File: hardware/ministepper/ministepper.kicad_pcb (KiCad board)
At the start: 4 copper layers, 0 parts

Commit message: hardware: scaffold ministepper (TMC2130 dual stepper driver) project
Third PCB in the family, matching firmware/tsumikoro-ministepper's
STM32G071G8U6 target. 4-layer, same JLC04161H stackup and design rules
as servo + bridge.

Placed (not wired):
- U1 STM32G071G8U6 UFQFPN-28 (core MCU)
- U2, U3 TMC2130-LA-T (shared SPI bus, per-driver CS/STEP/DIR/EN/DIAG)
- U4 SIT3088EEUA (RS-485, USART2 on PA2/PA3 — no SYSCFG remap needed on
  G071 unlike G030)
- JBUS1, JBUS2 (JST-XH 4-pin daisy-chain, V+/B/A/GND)
- JMOT1, JMOT2 (JST-XH 4-pin stepper outputs)
- JPWR (JST-XH 2-pin optional external motor supply)
- D1, D2 (SS34 Schottky diode-OR for bus V+ vs external)

PSU sub-sheet forked from servo's psu.kicad_sch — TPS54061 @ 3.3V,
sized for ~150 mA (MCU + 2x TMC VCC_IO + RS-485). UUIDs retargeted for
the ministepper project.

Docs README covers the full pin map, TMC2130 strapping checklist
(sense resistors, charge pump cap, VCP/5VOUT/VCC caps, DIAG pull-ups),
connectors, and regeneration commands.

Added hardware/TODO.md tracking servo/bridge/ministepper/light-sensor
projects with outstanding work per board.

Makefile PROJECTS list extended to servo bridge ministepper.
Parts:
- added C1: 2.2uF, Capacitor_SMD:C_1206_3216Metric, F.Cu at (170.7, 75.6)
- added C2: 100nF, Capacitor_SMD:C_0603_1608Metric, F.Cu at (169.9, 78.5)
- added C3: 100nF, Capacitor_SMD:C_0402_1005Metric, F.Cu at (160.9, 87.0)
- added C4: 10uF, Capacitor_SMD:C_0805_2012Metric, F.Cu at (167.3, 82.0)
- added C5: 10uF, Capacitor_SMD:C_0805_2012Metric, F.Cu at (167.3, 85.0)
- added D1: MBRD10200, Package_TO_SOT_SMD:TO-252-2, F.Cu at (152.2, 94.8)
- added D2: MBRD10200, Package_TO_SOT_SMD:TO-252-2, F.Cu at (152.2, 103.0)
- added JBUS1: Conn_01x04_XH, Connector_JST:JST_XH_S4B-XH-A_1x04_P2.50mm_Horizontal, F.Cu at (134.3, 94.0)
- added JBUS2: Conn_01x04_XH, Connector_JST:JST_XH_S4B-XH-A_1x04_P2.50mm_Horizontal, F.Cu at (134.3, 107.5)
- added JDC1: DC-005 2.0mm, Connector_BarrelJack:BarrelJack_GCT_DCJ200-10-A_Horizontal, F.Cu at (119.2, 75.9)
- added JDC2: DC-005 2.0mm, Connector_BarrelJack:BarrelJack_GCT_DCJ200-10-A_Horizontal, F.Cu at (131.6, 75.9)
- added JPTERM1: TERM1, Jumper:SolderJumper-2_P1.3mm_Open_Pad1.0x1.5mm, F.Cu at (154.7, 84.9)
- added JPTERM2: TERM2, Jumper:SolderJumper-2_P1.3mm_Open_Pad1.0x1.5mm, F.Cu at (154.7, 88.4)
- added J_USB2: USB-TYPE-C-019, Connector_USB:USB_C_Receptacle_GCT_USB4105-xx-A_16P_TopMnt_Horizontal, F.Cu at (151.1, 112.3)
- added L1: 10uH, Inductor_SMD:L_Changjiang_FNR4030S, F.Cu at (162.2, 83.3)
- added R1: 100k, Resistor_SMD:R_0402_1005Metric, F.Cu at (171.0, 81.5)
- added R2: 22k, Resistor_SMD:R_0402_1005Metric, F.Cu at (171.0, 83.5)
- added R3: 10k, Resistor_SMD:R_0402_1005Metric, F.Cu at (171.0, 85.5)
- added R4: 120R, Resistor_SMD:R_1206_3216Metric, F.Cu at (149.8, 84.8)
- added R5: 120R, Resistor_SMD:R_1206_3216Metric, F.Cu at (149.8, 88.1)
- added R_BOOT2: 10k, Resistor_SMD:R_0402_1005Metric, F.Cu at (155.8, 74.9)
- added R_CC1: 5.1k, Resistor_SMD:R_0402_1005Metric, F.Cu at (155.8, 76.9)
- added R_CC2: 5.1k, Resistor_SMD:R_0402_1005Metric, F.Cu at (155.8, 78.9)
- added R_EN2: 10k, Resistor_SMD:R_0402_1005Metric, F.Cu at (155.8, 80.9)
- added SW_BOOT2: BOOT, tsumikoro:SW_Push_1P1T_XKB_TS-1187A, F.Cu at (142.7, 77.2)
- added SW_RESET2: RESET, tsumikoro:SW_Push_1P1T_XKB_TS-1187A, F.Cu at (142.7, 83.9)
- added U1: SIT3088EEUA, Package_SO:MSOP-8_3x3mm_P0.65mm, F.Cu at (150.7, 76.2)
- added U2: LMR38020SDDAR, Package_SO:SOIC-8-1EP_3.9x4.9mm_P1.27mm_EP2.29x3mm, F.Cu at (163.6, 77.3)
- added U3: SIT3088EEUA, Package_SO:MSOP-8_3x3mm_P0.65mm, F.Cu at (150.7, 80.8)
- added U4: ESP32-S3-MINI-1-N8, tsumikoro:ESP32-S3-MINI-1, F.Cu at (186.6, 117.8)

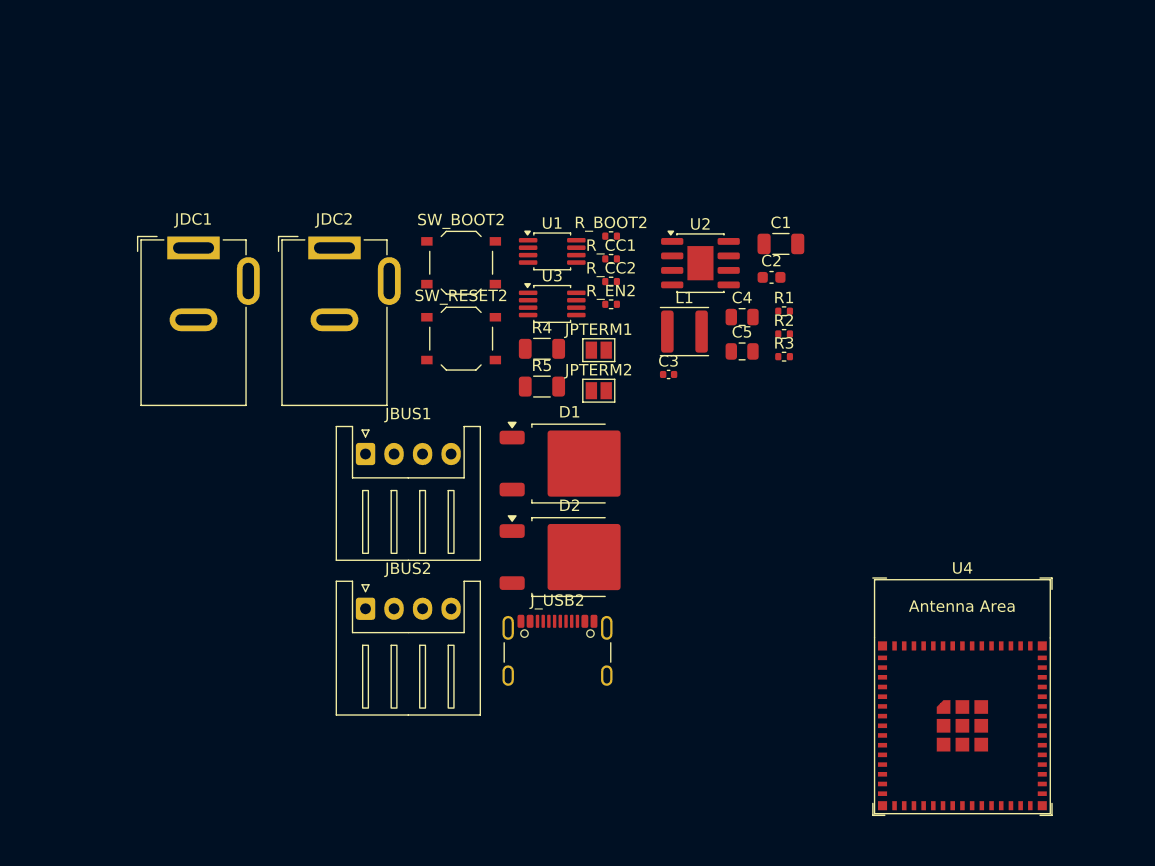
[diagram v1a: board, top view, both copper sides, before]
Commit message: ministepper: motor connectors (JMOT1, JMOT2) switch to vertical JST-XH
Was S4B-XH-A horizontal (right-angle, LCSC C157925) — now B4B-XH-A
vertical (top-mount, LCSC C595709, B4B-XH-A-R(LF)(SN), red housing
version, ~$0.08). The vertical variant keeps the motor cables exiting
straight up, which is usually more natural for stepper wiring vs the
board-edge horizontal style.

Bus connectors (JBUS1, JBUS2) and the optional external-power input
(JPWR) remain horizontal S*B-XH-A for board-edge cable exit.

Also regenerates docs + JLCPCB package.
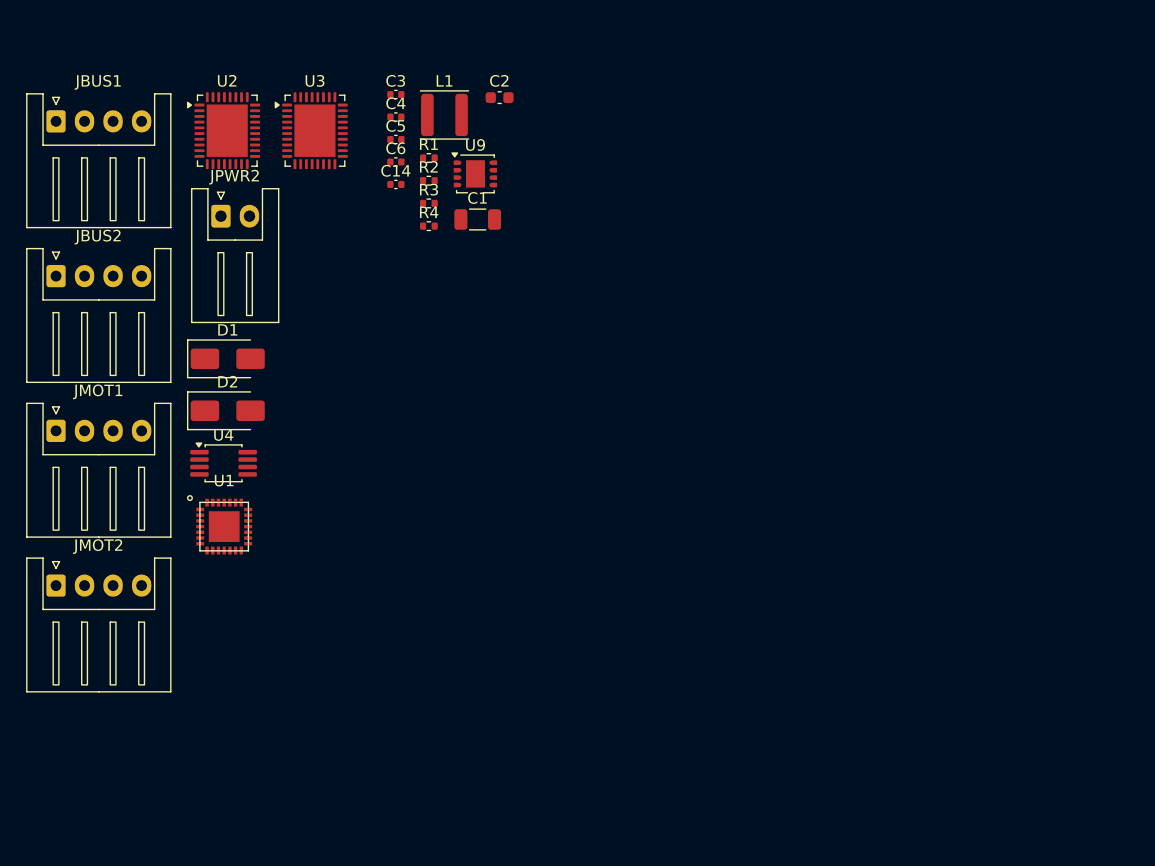
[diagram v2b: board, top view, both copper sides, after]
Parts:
- removed JDC1, JDC2: DC-005 2.0mm, Connector_BarrelJack:BarrelJack_GCT_DCJ200-10-A_Horizontal
- removed JPTERM1: TERM1, Jumper:SolderJumper-2_P1.3mm_Open_Pad1.0x1.5mm
- removed JPTERM2: TERM2, Jumper:SolderJumper-2_P1.3mm_Open_Pad1.0x1.5mm
- removed J_USB2: USB-TYPE-C-019, Connector_USB:USB_C_Receptacle_GCT_USB4105-xx-A_16P_TopMnt_Horizontal
- removed R5: 120R, Resistor_SMD:R_1206_3216Metric
- removed R_BOOT2, R_EN2: 10k, Resistor_SMD:R_0402_1005Metric
- removed R_CC1, R_CC2: 5.1k, Resistor_SMD:R_0402_1005Metric
- removed SW_BOOT2: BOOT, tsumikoro:SW_Push_1P1T_XKB_TS-1187A
- removed SW_RESET2: RESET, tsumikoro:SW_Push_1P1T_XKB_TS-1187A
- added C14: 10uF, Capacitor_SMD:C_0402_1005Metric, F.Cu at (137.0, 70.4)
- added C6: 33pF, Capacitor_SMD:C_0402_1005Metric, F.Cu at (137.0, 68.4)
- added JMOT1: Stepper 1, Connector_JST:JST_XH_S4B-XH-A_1x04_P2.50mm_Horizontal, F.Cu at (107.2, 92.0)
- added JMOT2: Stepper 2, Connector_JST:JST_XH_S4B-XH-A_1x04_P2.50mm_Horizontal, F.Cu at (107.2, 105.5)
- added JPWR2: Conn_01x02_XH, Connector_JST:JST_XH_S2B-XH-A_1x02_P2.50mm_Horizontal, F.Cu at (121.6, 73.1)
- added U9: TPS54061DRBT, Package_SON:Texas_S-PVSON-N8, F.Cu at (143.9, 69.4)
- C3: value 100nF -> 10nF
- C4: footprint Capacitor_SMD:C_0805_2012Metric -> Capacitor_SMD:C_0402_1005Metric
- C5: value 10uF -> 4.7nF; footprint Capacitor_SMD:C_0805_2012Metric -> Capacitor_SMD:C_0402_1005Metric
- D1, D2: value MBRD10200 -> SS34; footprint Package_TO_SOT_SMD:TO-252-2 -> Diode_SMD:D_SMA
- L1: value 10uH -> 100uH; footprint Inductor_SMD:L_Changjiang_FNR4030S -> Inductor_SMD:L_Sunlord_SWPA4018S
- R1: value 100k -> 143k
- R2: value 22k -> 31.6k
- R4: value 120R -> 26.1k; footprint Resistor_SMD:R_1206_3216Metric -> Resistor_SMD:R_0402_1005Metric
- U1: value SIT3088EEUA -> STM32G071G8U6; footprint Package_SO:MSOP-8_3x3mm_P0.65mm -> tsumikoro:UFQFPN-28
- U2: value LMR38020SDDAR -> TMC2130-LA; footprint Package_SO:SOIC-8-1EP_3.9x4.9mm_P1.27mm_EP2.29x3mm -> Package_DFN_QFN:QFN-36-1EP_5x6mm_P0.5mm_EP3.6x4.6mm
- U3: value SIT3088EEUA -> TMC2130-LA; footprint Package_SO:MSOP-8_3x3mm_P0.65mm -> Package_DFN_QFN:QFN-36-1EP_5x6mm_P0.5mm_EP3.6x4.6mm
- U4: value ESP32-S3-MINI-1-N8 -> SIT3088EEUA; footprint tsumikoro:ESP32-S3-MINI-1 -> Package_SO:MSOP-8_3x3mm_P0.65mm
- moved U4 68.7 mm to (121.9, 94.8)
- moved U2 43.1 mm to (122.2, 65.7)
- moved JBUS1 39.8 mm to (107.2, 64.8)
- moved JBUS2 39.8 mm to (107.2, 78.4)
- moved U1 37.5 mm to (121.9, 100.3)
- moved C5 35.6 mm to (137.0, 66.4)
- moved C4 35.0 mm to (137.0, 64.5)
- moved C3 34.2 mm to (137.0, 62.5)
- moved R1 33.9 mm to (139.8, 68.0)
- moved R2 33.9 mm to (139.8, 70.0)
- moved R3 33.9 mm to (139.8, 72.0)
- moved D2 32.6 mm to (122.2, 90.2)
- moved D1 31.3 mm to (122.2, 85.6)
- moved C2 28.6 mm to (146.0, 62.8)
- moved L1 28.3 mm to (141.2, 64.3)
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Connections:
- C1 pad 1: unconnected-(C1-Pad1) -> VPP
- C1 pad 2: unconnected-(C1-Pad2) -> GND
- C2 pad 1: unconnected-(C2-Pad1) -> VPP
- C2 pad 2: unconnected-(C2-Pad2) -> GND
- C3 pad 1: unconnected-(C3-Pad1) -> Net-(U9-BOOT)
- C3 pad 2: unconnected-(C3-Pad2) -> Net-(U9-PH)
- C4 pad 1: unconnected-(C4-Pad1) -> +3.3V
- C4 pad 2: unconnected-(C4-Pad2) -> GND
- C5 pad 1: unconnected-(C5-Pad1) -> Net-(C5-Pad1)
- C5 pad 2: unconnected-(C5-Pad2) -> GND
- L1 pad 1: unconnected-(L1-Pad1) -> Net-(U9-PH)
- L1 pad 2: unconnected-(L1-Pad2) -> +3.3V
- R1 pad 1: unconnected-(R1-Pad1) -> Net-(U9-RT/CLK)
- R1 pad 2: unconnected-(R1-Pad2) -> GND
- R2 pad 1: unconnected-(R2-Pad1) -> +3.3V
- R2 pad 2: unconnected-(R2-Pad2) -> Net-(U9-VSENSE)
- R3 pad 1: unconnected-(R3-Pad1) -> Net-(U9-VSENSE)
- R3 pad 2: unconnected-(R3-Pad2) -> GND
- R4 pad 1: unconnected-(R4-Pad1) -> Net-(U9-COMP)
- R4 pad 2: unconnected-(R4-Pad2) -> Net-(C5-Pad1)
- U4 pad 1: Net-(U4-GND-Pad1) -> unconnected-(U4-RO-Pad1)
- U4 pad 2: Net-(U4-GND-Pad1) -> unconnected-(U4-~{RE}-Pad2)

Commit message: pcb
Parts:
- added C_5VOUT2: 2.2uF, Capacitor_SMD:C_0603_1608Metric, F.Cu at (193.4, 70.6)
- added C_5VOUT3: 2.2uF, Capacitor_SMD:C_0603_1608Metric, F.Cu at (190.7, 125.0)
- added C_BRA_FILT2: 100nF, Capacitor_SMD:C_0402_1005Metric, F.Cu at (189.4, 62.6)
- added C_BRA_FILT3: 100nF, Capacitor_SMD:C_0402_1005Metric, F.Cu at (187.3, 112.2)
- added C_BRB_FILT2: 100nF, Capacitor_SMD:C_0402_1005Metric, F.Cu at (183.8, 78.0)
- added C_BRB_FILT3: 100nF, Capacitor_SMD:C_0402_1005Metric, F.Cu at (187.3, 114.2)
- added C_CP2: 22nF, Capacitor_SMD:C_0402_1005Metric, F.Cu at (191.4, 68.5)
- added C_CP3: 22nF, Capacitor_SMD:C_0402_1005Metric, F.Cu at (187.3, 116.1)
- added C_VCC2: 470nF, Capacitor_SMD:C_0603_1608Metric, F.Cu at (193.4, 69.0)
- added C_VCC3: 470nF, Capacitor_SMD:C_0603_1608Metric, F.Cu at (190.7, 127.5)
- added C_VCC_IO2: 100nF, Capacitor_SMD:C_0402_1005Metric, F.Cu at (182.2, 72.5)
- added C_VCC_IO3: 100nF, Capacitor_SMD:C_0402_1005Metric, F.Cu at (187.3, 118.1)
- added C_VCP2: 100nF, Capacitor_SMD:C_0402_1005Metric, F.Cu at (189.6, 66.2)
- added C_VCP3: 100nF, Capacitor_SMD:C_0402_1005Metric, F.Cu at (187.3, 120.1)
- added C_VS2: 100nF, Capacitor_SMD:C_0402_1005Metric, F.Cu at (189.1, 76.6)
- added C_VS3: 100nF, Capacitor_SMD:C_0402_1005Metric, F.Cu at (187.3, 122.0)
- added C_VSA2: 100nF, Capacitor_SMD:C_0402_1005Metric, F.Cu at (189.6, 65.2)
- added C_VSA3: 100nF, Capacitor_SMD:C_0402_1005Metric, F.Cu at (187.3, 124.0)
- added C_VS_BULK2: 10uF, Capacitor_SMD:C_1210_3225Metric, F.Cu at (191.2, 78.0)
- added C_VS_BULK3: 10uF, Capacitor_SMD:C_1210_3225Metric, F.Cu at (191.5, 121.6)
- added RSA2: 0.1R, Resistor_SMD:R_1210_3225Metric, F.Cu at (187.0, 62.6)
- added RSA3: 0.1R, Resistor_SMD:R_1210_3225Metric, F.Cu at (183.0, 113.3)
- added RSB2: 0.1R, Resistor_SMD:R_1210_3225Metric, F.Cu at (186.4, 78.0)
- added RSB3: 0.1R, Resistor_SMD:R_1210_3225Metric, F.Cu at (183.0, 121.7)
- added R_DIAG1: 47k, Resistor_SMD:R_0402_1005Metric, F.Cu at (192.2, 71.8)
- added R_DIAG2: 47k, Resistor_SMD:R_0402_1005Metric, F.Cu at (194.2, 124.8)
- added R_VCC2: 2.2, Resistor_SMD:R_0402_1005Metric, F.Cu at (191.4, 70.4)
- added R_VCC3: 2.2, Resistor_SMD:R_0402_1005Metric, F.Cu at (194.2, 126.7)
- JMOT1, JMOT2: footprint Connector_JST:JST_XH_S4B-XH-A_1x04_P2.50mm_Horizontal -> Connector_JST:JST_XH_B4B-XH-A_1x04_P2.50mm_Vertical
- moved U3 80.1 mm to (192.7, 115.4)
- moved U2 64.8 mm to (186.8, 70.7)
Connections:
- U2 pad 1: unconnected-(U2-CLK-Pad1) -> GND
- U2 pad 10: unconnected-(U2-SPI_MODE-Pad10) -> +3.3V
- U2 pad 12: unconnected-(U2-GNDP-Pad12) -> GND
- U2 pad 13: unconnected-(U2-OB1-Pad13) -> /Stepper 1/MOT_B+
- U2 pad 14: unconnected-(U2-BRB-Pad14) -> Net-(U2-BRB)
- U2 pad 15: unconnected-(U2-OB2-Pad15) -> /Stepper 1/MOT_B-
- U2 pad 16: unconnected-(U2-VS-Pad16) -> VPP
- U2 pad 18: unconnected-(U2-DCEN-Pad18) -> GND
- U2 pad 19: unconnected-(U2-DCIN-Pad19) -> GND
- U2 pad 2: unconnected-(U2-CSN-Pad2) -> /Stepper 1/CS
- U2 pad 21: unconnected-(U2-DIAG1-Pad21) -> /Stepper 1/DIAG1
- U2 pad 22: unconnected-(U2-DRV_ENN-Pad22) -> /Stepper 1/DRV_ENN
- U2 pad 24: unconnected-(U2-GNDA-Pad24) -> GND
- U2 pad 25: unconnected-(U2-5VOUT-Pad25) -> Net-(U2-5VOUT)
- U2 pad 26: unconnected-(U2-VCC-Pad26) -> /Stepper 1/5VOUT
- U2 pad 27: unconnected-(U2-CPO-Pad27) -> Net-(U2-CPO)
- U2 pad 28: unconnected-(U2-CPI-Pad28) -> Net-(U2-CPI)
- U2 pad 29: unconnected-(U2-VCP-Pad29) -> /Stepper 1/VCP
- U2 pad 3: unconnected-(U2-SCK-Pad3) -> /Stepper 1/SCK
- U2 pad 30: unconnected-(U2-VSA-Pad30) -> VPP
- U2 pad 31: unconnected-(U2-VS_2-Pad31) -> VPP
- U2 pad 32: unconnected-(U2-OA2-Pad32) -> /Stepper 1/MOT_A-
- U2 pad 33: unconnected-(U2-BRA-Pad33) -> Net-(U2-BRA)
- U2 pad 34: unconnected-(U2-OA1-Pad34) -> /Stepper 1/MOT_A+
- U2 pad 35: unconnected-(U2-GNDP_2-Pad35) -> GND
- U2 pad 36: unconnected-(U2-TST_MODE-Pad36) -> GND
- U2 pad 37: unconnected-(U2-EP-Pad37) -> GND
- U2 pad 4: unconnected-(U2-SDI-Pad4) -> /Stepper 1/MOSI
- U2 pad 5: unconnected-(U2-SDO-Pad5) -> /Stepper 1/MISO
- U2 pad 6: unconnected-(U2-STEP-Pad6) -> /Stepper 1/STEP
- U2 pad 7: unconnected-(U2-DIR-Pad7) -> /Stepper 1/DIR
- U2 pad 8: unconnected-(U2-VCC_IO-Pad8) -> +3.3V
- U3 pad 1: unconnected-(U3-CLK-Pad1) -> GND
- U3 pad 10: unconnected-(U3-SPI_MODE-Pad10) -> +3.3V
- U3 pad 12: unconnected-(U3-GNDP-Pad12) -> GND
- U3 pad 13: unconnected-(U3-OB1-Pad13) -> /Stepper 2/MOT_B+
- U3 pad 14: unconnected-(U3-BRB-Pad14) -> Net-(U3-BRB)
- U3 pad 15: unconnected-(U3-OB2-Pad15) -> /Stepper 2/MOT_B-
- U3 pad 16: unconnected-(U3-VS-Pad16) -> VPP
- U3 pad 18: unconnected-(U3-DCEN-Pad18) -> GND
- U3 pad 19: unconnected-(U3-DCIN-Pad19) -> GND
- U3 pad 2: unconnected-(U3-CSN-Pad2) -> /Stepper 2/CS
- U3 pad 21: unconnected-(U3-DIAG1-Pad21) -> /Stepper 2/DIAG1
- U3 pad 22: unconnected-(U3-DRV_ENN-Pad22) -> /Stepper 2/DRV_ENN
- U3 pad 24: unconnected-(U3-GNDA-Pad24) -> GND
- U3 pad 25: unconnected-(U3-5VOUT-Pad25) -> Net-(U3-5VOUT)
- U3 pad 26: unconnected-(U3-VCC-Pad26) -> /Stepper 2/5VOUT
- U3 pad 27: unconnected-(U3-CPO-Pad27) -> Net-(U3-CPO)
- U3 pad 28: unconnected-(U3-CPI-Pad28) -> Net-(U3-CPI)
- U3 pad 29: unconnected-(U3-VCP-Pad29) -> /Stepper 2/VCP
- U3 pad 3: unconnected-(U3-SCK-Pad3) -> /Stepper 2/SCK
- U3 pad 30: unconnected-(U3-VSA-Pad30) -> VPP
- U3 pad 31: unconnected-(U3-VS_2-Pad31) -> VPP
- U3 pad 32: unconnected-(U3-OA2-Pad32) -> /Stepper 2/MOT_A-
- U3 pad 33: unconnected-(U3-BRA-Pad33) -> Net-(U3-BRA)
- U3 pad 34: unconnected-(U3-OA1-Pad34) -> /Stepper 2/MOT_A+
- U3 pad 35: unconnected-(U3-GNDP_2-Pad35) -> GND
- U3 pad 36: unconnected-(U3-TST_MODE-Pad36) -> GND
- U3 pad 37: unconnected-(U3-EP-Pad37) -> GND
- U3 pad 4: unconnected-(U3-SDI-Pad4) -> /Stepper 2/MOSI
- U3 pad 5: unconnected-(U3-SDO-Pad5) -> /Stepper 2/MISO
- U3 pad 6: unconnected-(U3-STEP-Pad6) -> /Stepper 2/STEP
- U3 pad 7: unconnected-(U3-DIR-Pad7) -> /Stepper 2/DIR
- U3 pad 8: unconnected-(U3-VCC_IO-Pad8) -> +3.3V
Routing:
- net GND: track 0.00 -> 7.25 mm, vias 0 -> 1
- net VPP: track 0.00 -> 5.48 mm
- net Net-(U2-5VOUT): track 0.00 -> 4.02 mm
- net /Stepper 1/5VOUT: track 0.00 -> 3.96 mm
- net /Stepper 1/DIAG1: track 0.00 -> 3.23 mm
- net Net-(U2-BRB): track 0.00 -> 3.01 mm
- net Net-(U2-BRA): track 0.00 -> 2.81 mm
- net /Stepper 1/VCP: track 0.00 -> 2.71 mm
- net Net-(U2-CPI): track 0.00 -> 2.38 mm
- net Net-(U2-CPO): track 0.00 -> 2.24 mm
- net /Stepper 1/DRV_ENN: track 0.00 -> 1.25 mm, vias 0 -> 1
